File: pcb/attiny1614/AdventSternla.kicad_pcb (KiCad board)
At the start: 2 copper layers, 35.6 x 22.4 mm, 17 parts, among them J101 UPDI, J102 NeoPixel Data, J103 Power Out, J104 5V In, J105 GPIO_A, J106 GPIO_B, J107 GPIO_C, U101 ATTINY1614

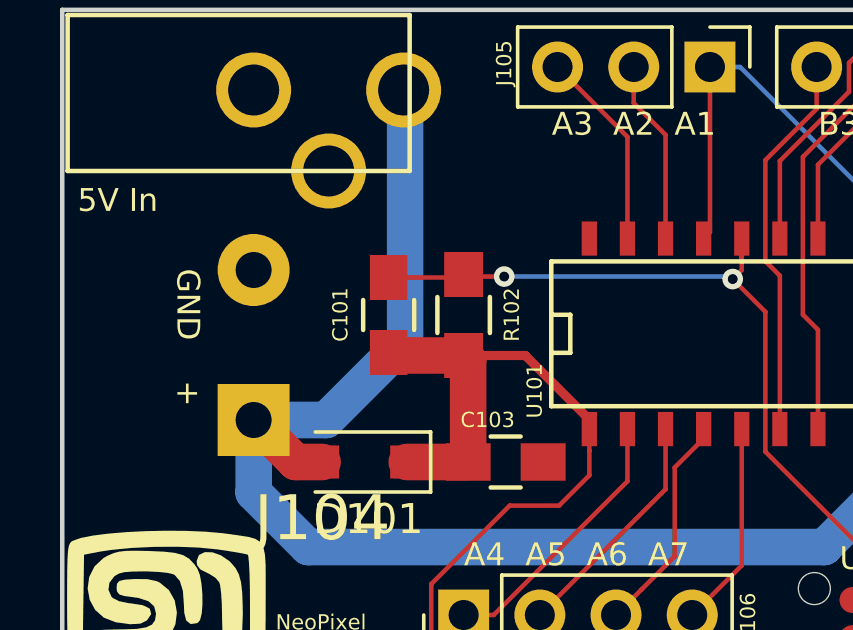
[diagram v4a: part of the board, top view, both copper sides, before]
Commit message: Made the layout change for the unneeded C101
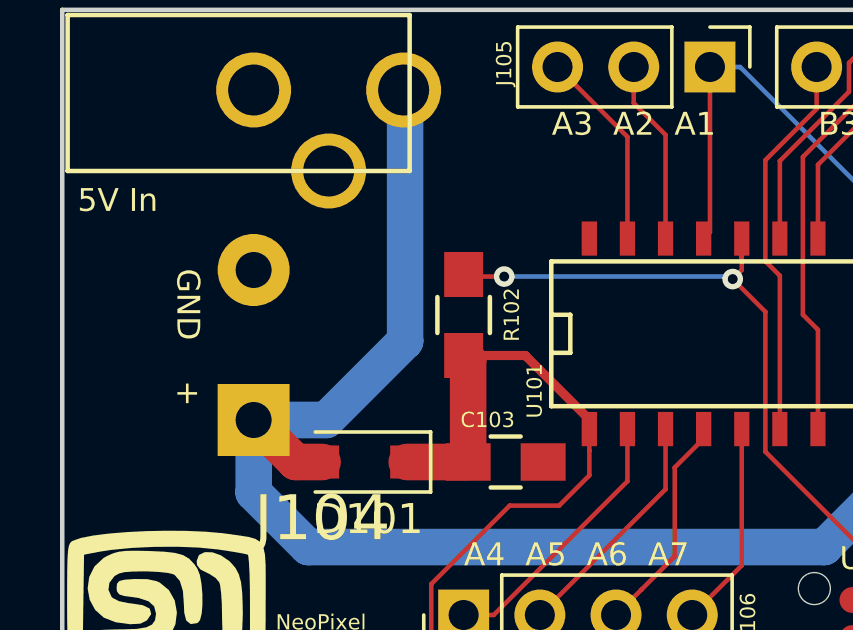
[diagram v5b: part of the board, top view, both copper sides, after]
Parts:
- removed C101: 100nF 50V, Capacitors_SMD:C_0805_HandSoldering
- R101: value 4k7Ω -> 470Ω
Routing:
- net /VDD: track 41.4 -> 38.8 mm
- net /PDI_DATA: track 27.5 -> 25.1 mm
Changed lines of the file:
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@@
 (kicad_pcb (version 4) (host pcbnew 4.0.7)
   (general
-    (links 30)
+    (links 28)
     (no_connects 0)
     (area 134.544999 84.252999 170.255001 106.755001)
     (thickness 1.6)
     (drawings 13)
-    (tracks 100)
+    (tracks 97)
     (zones 0)
-    (modules 17)
+    (modules 16)
     (nets 17)
   )
@@
   )
   (setup
-    (last_trace_width 1.2192)
+    (last_trace_width 0.1524)
     (user_trace_width 0.3048)
     (user_trace_width 0.6096)
@@
   )
   (module Capacitors_SMD:C_0805_HandSoldering (layer F.Cu)
-    (at 145.5 94.5 90)
-    (descr "Capacitor SMD 0805, hand soldering")
-    (tags "capacitor 0805")
-    (attr smd)
-    (fp_text reference C101 (at 0.012 -1.609 90) (layer F.SilkS)
-      (effects (font (size 0.508 0.508) (thickness 0.127)))
-    )
-    (fp_text value "100nF 50V" (at 0 2.1 90) (layer F.Fab)
-      (effects (font (size 0.508 0.508) (thickness 0.127)))
-    )
-    (fp_line (start -1 0.625) (end -1 -0.625) (layer F.Fab) (width 0.15))
-    (fp_line (start 1 0.625) (end -1 0.625) (layer F.Fab) (width 0.15))
-    (fp_line (start 1 -0.625) (end 1 0.625) (layer F.Fab) (width 0.15))
-    (fp_line (start -1 -0.625) (end 1 -0.625) (layer F.Fab) (width 0.15))
-    (fp_line (start -2.3 -1) (end 2.3 -1) (layer F.CrtYd) (width 0.05))
-    (fp_line (start -2.3 1) (end 2.3 1) (layer F.CrtYd) (width 0.05))
-    (fp_line (start -2.3 -1) (end -2.3 1) (layer F.CrtYd) (width 0.05))
-    (fp_line (start 2.3 -1) (end 2.3 1) (layer F.CrtYd) (width 0.05))
-    (fp_line (start 0.5 -0.85) (end -0.5 -0.85) (layer F.SilkS) (width 0.15))
-    (fp_line (start -0.5 0.85) (end 0.5 0.85) (layer F.SilkS) (width 0.15))
-    (pad 1 smd rect (at -1.25 0 90) (size 1.5 1.25) (layers F.Cu F.Paste F.Mask)
-      (net 3 /VDD))
-    (pad 2 smd rect (at 1.25 0 90) (size 1.5 1.25) (layers F.Cu F.Paste F.Mask)
-      (net 4 /PDI_DATA))
-    (model Capacitors_SMD.3dshapes/C_0805_HandSoldering.wrl
-      (at (xyz 0 0 0))
-      (scale (xyz 1 1 1))
-      (rotate (xyz 0 0 0))
-    )
-  )
-  (module Capacitors_SMD:C_0805_HandSoldering (layer F.Cu)
     (at 149.4 99.4)
     (descr "Capacitor SMD 0805, hand soldering")
@@
       (effects (font (size 0.508 0.508) (thickness 0.127)))
     )
-    (fp_text value 4k7Ω (at 0 2.1) (layer F.Fab)
+    (fp_text value 470Ω (at 0 2.1) (layer F.Fab)
       (effects (font (size 0.508 0.508) (thickness 0.127)))
     )
@@
   (gr_line (start 170.18 84.328) (end 170.18 106.68) (angle 90) (layer Edge.Cuts) (width 0.15))
   (gr_line (start 134.62 84.328) (end 170.18 84.328) (angle 90) (layer Edge.Cuts) (width 0.15))
-  (segment (start 141 98) (end 142.4 99.4) (width 1.2192) (layer F.Cu) (net 1) (status 400000))
-  (segment (start 142.4 99.4) (end 143.3 99.4) (width 1.2192) (layer F.Cu) (net 1) (status 800000))
+  (segment (start 141 98) (end 142.4 99.4) (width 1.2192) (layer F.Cu) (net 1))
+  (segment (start 142.4 99.4) (end 143.3 99.4) (width 1.2192) (layer F.Cu) (net 1))
   (segment (start 146.05 87.122) (end 146.05 95.3692) (width 1.2192) (layer B.Cu) (net 1))
   (segment (start 146.05 95.3692) (end 143.4192 98) (width 1.2192) (layer B.Cu) (net 1))
@@
   (segment (start 167.85 98) (end 167.894 98.044) (width 1.2192) (layer B.Cu) (net 1))
   (segment (start 141 98) (end 141.45 98) (width 1.2192) (layer F.Cu) (net 1))
-  (segment (start 148 95.85) (end 148.15 96) (width 1.2192) (layer F.Cu) (net 3) (status C00000))
-  (segment (start 148.15 96) (end 148.15 99.4) (width 1.2192) (layer F.Cu) (net 3) (status C00000))
-  (segment (start 146.1 99.4) (end 148.15 99.4) (width 1.2192) (layer F.Cu) (net 3) (status C00000))
+  (segment (start 148 95.85) (end 148.15 96) (width 1.2192) (layer F.Cu) (net 3))
+  (segment (start 148.15 96) (end 148.15 99.4) (width 1.2192) (layer F.Cu) (net 3))
+  (segment (start 146.1 99.4) (end 148.15 99.4) (width 1.2192) (layer F.Cu) (net 3))
   (segment (start 163.5 105.27) (end 162.356999 106.413001) (width 0.1524) (layer F.Cu) (net 3))
   (segment (start 162.356999 106.413001) (end 147.801519 106.413001) (width 0.1524) (layer F.Cu) (net 3))
@@
   (segment (start 150.0555 95.85) (end 152.19 97.9845) (width 0.3048) (layer F.Cu) (net 3))
   (segment (start 152.19 97.9845) (end 152.19 98.302) (width 0.3048) (layer F.Cu) (net 3))
-  (segment (start 148 95.85) (end 145.6 95.85) (width 1.2192) (layer F.Cu) (net 3))
-  (segment (start 145.6 95.85) (end 145.5 95.75) (width 1.2192) (layer F.Cu) (net 3))
   (segment (start 163.5 104) (end 162.839599 103.339599) (width 0.1524) (layer F.Cu) (net 4))
   (segment (start 162.340617 103.339599) (end 158.057399 99.056381) (width 0.1524) (layer F.Cu) (net 4))
@@
   (segment (start 148.068 93.218) (end 148 93.15) (width 0.1524) (layer F.Cu) (net 4))
   (via (at 149.352 93.218) (size 0.6858) (drill 0.3302) (layers F.Cu B.Cu) (net 4))
-  (segment (start 145.5 93.25) (end 147.9 93.25) (width 0.1524) (layer F.Cu) (net 4))
   (segment (start 147.9 93.25) (end 148 93.15) (width 0.1524) (layer F.Cu) (net 4))
   (segment (start 157.27 92.6759) (end 157.27 91.952) (width 0.1524) (layer F.Cu) (net 4))

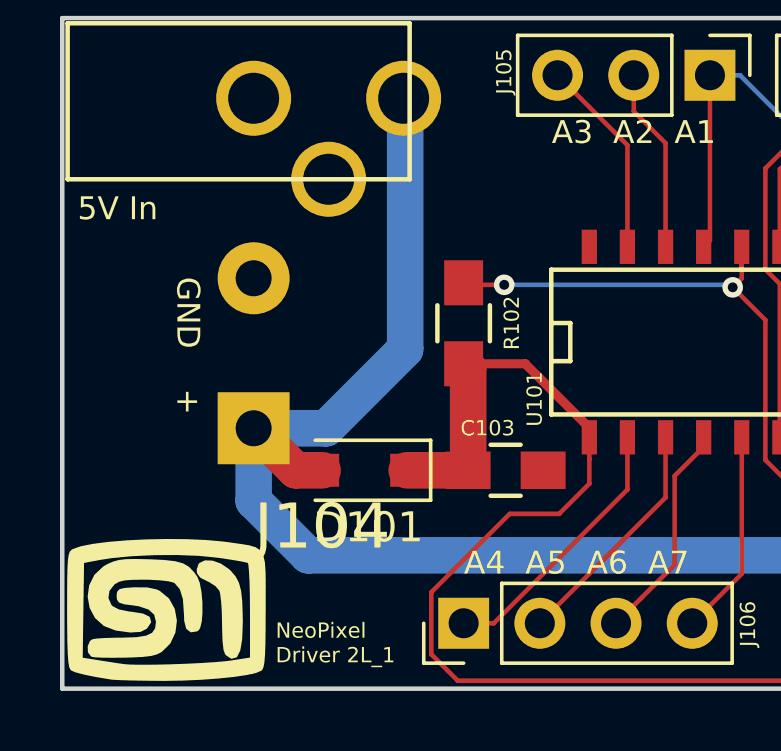
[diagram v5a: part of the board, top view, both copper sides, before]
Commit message: Fixed up the diode foot print
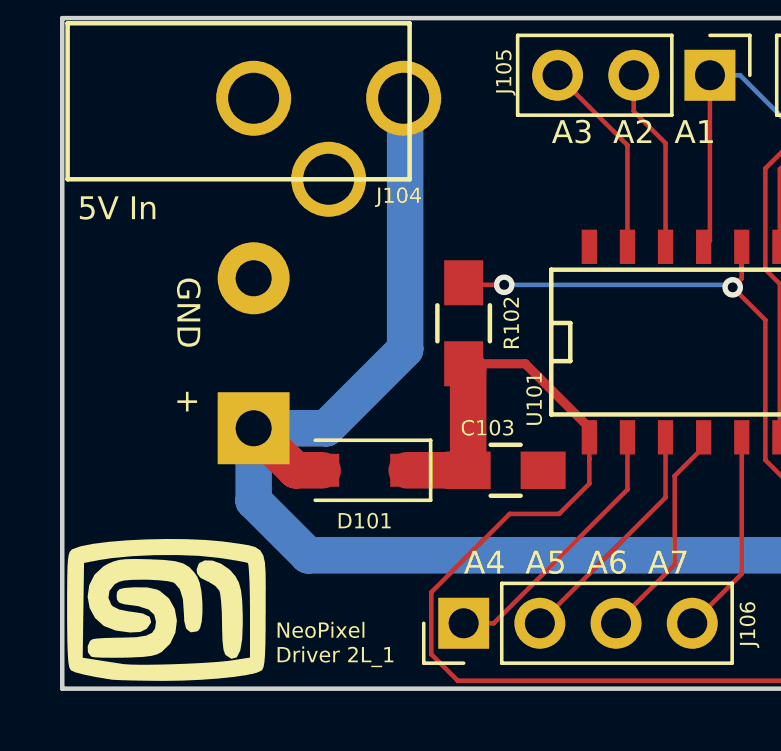
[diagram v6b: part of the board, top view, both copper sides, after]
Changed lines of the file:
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@@
     (at 163.83 104.267 180)
     (fp_text reference G*** (at 0 0 180) (layer B.SilkS) hide
-      (effects (font (thickness 0.3)) (justify mirror))
+      (effects (font (size 0.508 0.508) (thickness 0.127)) (justify mirror))
     )
     (fp_text value LOGO (at 0.75 0 180) (layer B.SilkS) hide
-      (effects (font (thickness 0.3)) (justify mirror))
+      (effects (font (size 0.508 0.508) (thickness 0.127)) (justify mirror))
     )
     (fp_poly (pts (xy 3.701898 -1.159053) (xy 3.700458 -1.349921) (xy 3.700334 -1.358623) (xy 3.693583 -1.82407)
@@
     (tags "CP Radal series Radial Horizontal pin pitch 5mm  length 21mm diameter 13mm Electrolytic Capacitor")
     (fp_text reference C102 (at 14 0) (layer B.SilkS)
-      (effects (font (size 1 1) (thickness 0.15)) (justify mirror))
+      (effects (font (size 0.508 0.508) (thickness 0.127)) (justify mirror))
     )
     (fp_text value "1000μF 25V" (at 14 -5.06) (layer B.Fab)
-      (effects (font (size 1 1) (thickness 0.15)) (justify mirror))
+      (effects (font (size 0.508 0.508) (thickness 0.127)) (justify mirror))
     )
     (fp_line (start 0 -2.5) (end 3.5 -2.5) (layer B.Fab) (width 0.1))
@@
     (fp_line (start 25 7) (end -1.45 7) (layer B.CrtYd) (width 0.05))
     (fp_text user %R (at 14 0) (layer B.Fab)
-      (effects (font (size 1 1) (thickness 0.15)) (justify mirror))
+      (effects (font (size 0.508 0.508) (thickness 0.127)) (justify mirror))
     )
     (pad 1 thru_hole rect (at 0 2.5) (size 2.4 2.4) (drill 1.2) (layers *.Cu *.Mask)
@@
     (at 143.5 87)
     (descr "CONN PWR JACK 1.3X3.5MM SOLDER")
-    (fp_text reference J104 (at -0.21 14.28) (layer F.SilkS)
-      (effects (font (size 1.5 1.5) (thickness 0.15)))
+    (fp_text reference J104 (at 2.35 3.25) (layer F.SilkS)
+      (effects (font (size 0.508 0.508) (thickness 0.127)))
     )
     (fp_text value "5V In" (at 0.02 -13.49) (layer F.Fab)
-      (effects (font (size 1.5 1.5) (thickness 0.15)))
+      (effects (font (size 0.508 0.508) (thickness 0.127)))
     )
     (fp_line (start -8.9 4.1) (end -8.9 -2.7) (layer F.CrtYd) (width 0.15))
@@
     (tags D_SOD-123F)
     (attr smd)
-    (fp_text reference D101 (at -0.127 -1.905 180) (layer F.SilkS)
-      (effects (font (size 1 1) (thickness 0.15)))
+    (fp_text reference D101 (at 0 -1.7 180) (layer F.SilkS)
+      (effects (font (size 0.508 0.508) (thickness 0.127)))
     )
     (fp_text value 1N4148WSTR (at 0 2.1 180) (layer F.Fab)
-      (effects (font (size 1 1) (thickness 0.15)))
+      (effects (font (size 0.508 0.508) (thickness 0.127)))
     )
     (fp_text user %R (at -0.127 -1.905 180) (layer F.Fab)
-      (effects (font (size 1 1) (thickness 0.15)))
+      (effects (font (size 0.508 0.508) (thickness 0.127)))
     )
     (fp_line (start -2.2 -1) (end -2.2 1) (layer F.SilkS) (width 0.12))
